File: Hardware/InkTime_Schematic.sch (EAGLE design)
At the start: 105 parts, among them IC1 RT6160AWSC, IC2 BMA423, IC3 BQ25180YBGR, IC4 DRV2605YZFR, J1 TC2030-IDC, J2 503480-2400, J4 KH-TYPE-C-16P_KH-TYPE-C-16P, Q1 20V/4.2A/52mΩ/1.4W, Q3 SI1308EDL-T1-GE3, U1 MAX17048G+T10, X1 32MHZ, X2 32.768KHZ

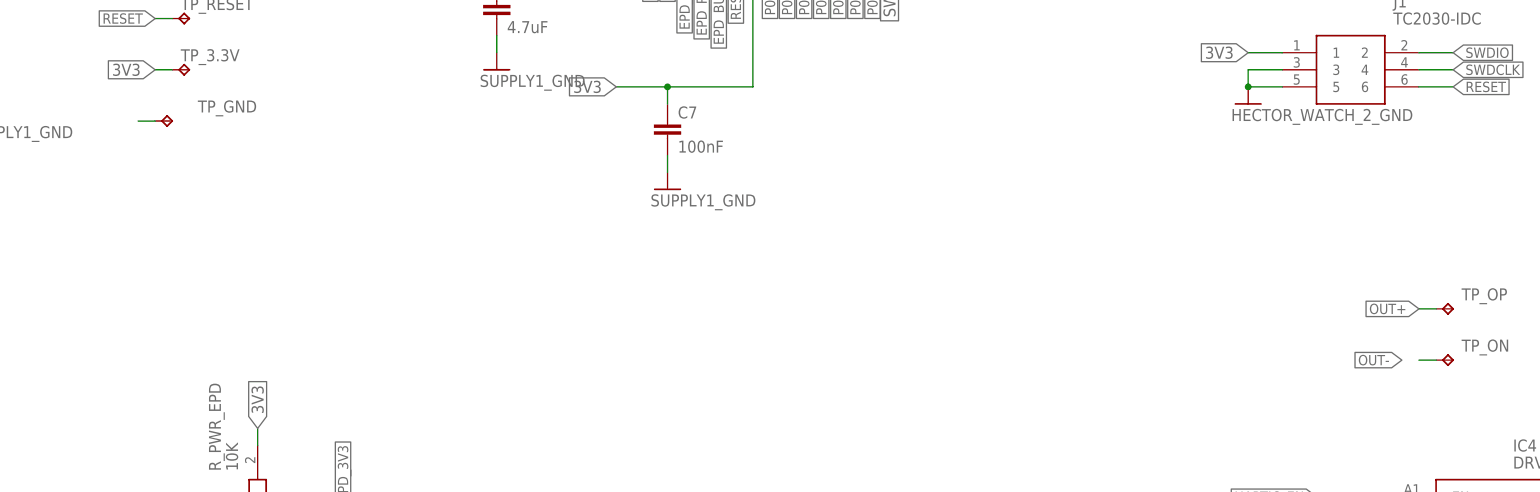
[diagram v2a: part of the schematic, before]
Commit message: Upated routing. Fixes #2, fixes #3, fixes #4, and resolves #5
Signed-off-by: Andrei Rusanescu <andreirusanescu154@gmail.com>
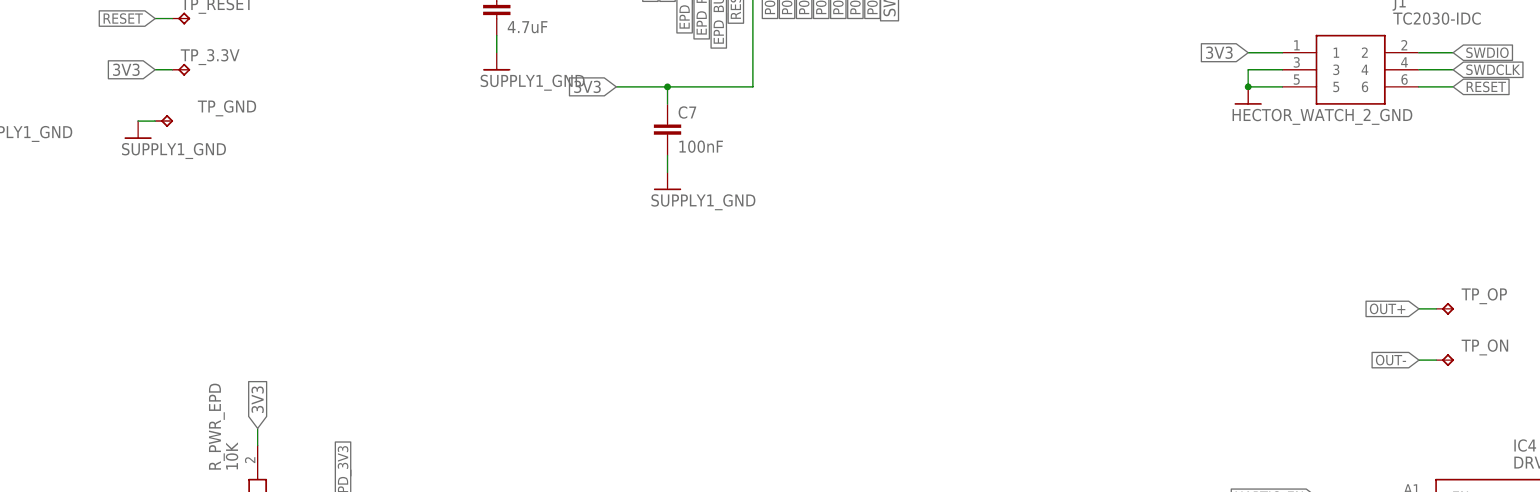
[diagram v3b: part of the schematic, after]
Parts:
- C19: SPICEPREFIX (none) -> C
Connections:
- removed net N$8: TP_GND.TP
- net GND: now also TP_GND.TP
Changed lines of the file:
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@@
 </classes>
 <parts>
-<part name="NRF52840_QF" library="InkTime_v5" deviceset="NORDIC_NRF_4_NRF52840_QF" device="" value="NRF52840_QF"/>
+<part uuid="0xABCDEF1A" name="NRF52840_QF" library="InkTime_v5" deviceset="NORDIC_NRF_4_NRF52840_QF" device="" value="NRF52840_QF"/>
 <part name="L1" library="InkTime_v5" deviceset="MLP2016SR47MT0S1_FTC252012SR47MBCA" device="" value="3.9nH"/>
 <part name="L2" library="InkTime_v5" deviceset="MLP2016SR47MT0S1_FTC252012SR47MBCA" device="" value="10uH"/>
 <part name="L3" library="InkTime_v5" deviceset="MLP2016SR47MT0S1_FTC252012SR47MBCA" device="" value="15nH"/>
-<part name="X1" library="InkTime_v5" deviceset="NORDIC_NRF_XTAL_32MHZ" device="" value="32MHZ"/>
+<part uuid="0xABCDEF0F" name="X1" library="InkTime_v5" deviceset="NORDIC_NRF_XTAL_32MHZ" device="" value="32MHZ"/>
 <part name="X2" library="InkTime_v5" deviceset="NORDIC_NRF_1_XTAL_32KHZ" device="" value="32.768KHZ"/>
-<part name="ANT1" library="InkTime_v5" deviceset="2450AT18B100E_2450AT18B100E" device="" value="2450AT18B100E"/>
-<part name="J1" library="InkTime_v5" deviceset="TC2030-IDC_TC2030-IDC" device="" value="TC2030-IDC"/>
-<part name="IC1" library="InkTime_v5" deviceset="RT6160AWSC_RT6160AWSC" device="" value="RT6160AWSC"/>
+<part uuid="0xABCDEF09" name="ANT1" library="InkTime_v5" deviceset="2450AT18B100E_2450AT18B100E" device="" value="2450AT18B100E"/>
+<part uuid="0xABCDEF18" name="J1" library="InkTime_v5" deviceset="TC2030-IDC_TC2030-IDC" device="" value="TC2030-IDC"/>
+<part uuid="0xABCDEF1C" name="IC1" library="InkTime_v5" deviceset="RT6160AWSC_RT6160AWSC" device="" value="RT6160AWSC"/>
 <part name="GND23" library="InkTime_v5" deviceset="HECTOR_WATCH_2_GND" device="" value="GND"/>
 <part name="R1" library="InkTime_v5" deviceset="CPF0201D7K68C1_CPF0201D7K68C1" device="" value="0"/>
@@
 <part name="TP_3.3V" library="InkTime_v5" deviceset="HECTOR_WATCH_1_TP" device="TP20R"/>
 <part name="TP_GND" library="InkTime_v5" deviceset="HECTOR_WATCH_1_TP" device="TP20R"/>
-<part name="IC2" library="InkTime_v5" deviceset="BMA423_BMA423" device="" value="BMA423"/>
+<part uuid="0xABCDEF1E" name="IC2" library="InkTime_v5" deviceset="BMA423_BMA423" device="" value="BMA423"/>
 <part name="R5" library="InkTime_v5" deviceset="CPF0201D7K68C1_CPF0201D7K68C1" device="" value="0"/>
-<part name="IC3" library="InkTime_v5" deviceset="BQ25180YBGR_BQ25180YBGR" device="" value="BQ25180YBGR"/>
+<part uuid="0xABCDEF02" name="IC3" library="InkTime_v5" deviceset="BQ25180YBGR_BQ25180YBGR" device="" value="BQ25180YBGR"/>
 <part name="R6" library="InkTime_v5" deviceset="CPF0201D7K68C1_CPF0201D7K68C1" device="" value="10K"/>
-<part name="D4" library="InkTime_v5" deviceset="ESP32_C6_LIBRARY_5_MBR0530" device="" value="MBR0530"/>
-<part name="D5" library="InkTime_v5" deviceset="ESP32_C6_LIBRARY_5_MBR0530" device="" value="MBR0530"/>
-<part name="D2" library="InkTime_v5" deviceset="ESP32_C6_LIBRARY_5_MBR0530" device="" value="MBR0530"/>
+<part uuid="0xABCDEF01" name="D4" library="InkTime_v5" deviceset="ESP32_C6_LIBRARY_5_MBR0530" device="" value="MBR0530"/>
+<part uuid="0xABCDEF05" name="D5" library="InkTime_v5" deviceset="ESP32_C6_LIBRARY_5_MBR0530" device="" value="MBR0530"/>
+<part uuid="0xABCDEF07" name="D2" library="InkTime_v5" deviceset="ESP32_C6_LIBRARY_5_MBR0530" device="" value="MBR0530"/>
 <part name="L5" library="InkTime_v5" deviceset="MLP2016SR47MT0S1_FTC252012SR47MBCA" device="" value="68uH"/>
-<part name="Q3" library="InkTime_v5" deviceset="ESP32_C6_LIBRARY_6_SI1308EDL-T1-GE3" device="" value="SI1308EDL-T1-GE3"/>
+<part uuid="0xABCDEF0B" name="Q3" library="InkTime_v5" deviceset="ESP32_C6_LIBRARY_6_SI1308EDL-T1-GE3" device="" value="SI1308EDL-T1-GE3"/>
 <part name="R2_EP_DR" library="InkTime_v5" deviceset="CPF0201D7K68C1_CPF0201D7K68C1" device="" value="10K"/>
 <part name="R1_EP_DR" library="InkTime_v5" deviceset="CPF0201D7K68C1_CPF0201D7K68C1" device="" value="0.47"/>
@@
 <part name="SJ1" library="InkTime_v5" deviceset="ESP32_C6_LIBRARY_7_JUMPER_SJ" device=""/>
 <part name="R_TYPE_SEL" library="InkTime_v5" deviceset="CPF0201D7K68C1_CPF0201D7K68C1" device="" value="2.2"/>
-<part name="Q1" library="InkTime_v5" deviceset="ESP32_C6_LIBRARY_4_ESP32_WROVER_SPARKFUN-DISCRETESEMI_MOSFET_PCH" device="-DMG2305UX-7" value="20V/4.2A/52mΩ/1.4W"/>
+<part uuid="0xABCDEF0D" name="Q1" library="InkTime_v5" deviceset="ESP32_C6_LIBRARY_4_ESP32_WROVER_SPARKFUN-DISCRETESEMI_MOSFET_PCH" device="-DMG2305UX-7" value="20V/4.2A/52mΩ/1.4W"/>
 <part name="R_PWR_EPD" library="InkTime_v5" deviceset="CPF0201D7K68C1_CPF0201D7K68C1" device="" value="10K"/>
-<part name="IC4" library="InkTime_v5" deviceset="DRV2605YZFR_DRV2605YZFR" device="" value="DRV2605YZFR"/>
+<part uuid="0xABCDEF14" name="IC4" library="InkTime_v5" deviceset="DRV2605YZFR_DRV2605YZFR" device="" value="DRV2605YZFR"/>
 <part name="TP_OP" library="InkTime_v5" deviceset="HECTOR_WATCH_1_TP" device="TP20R"/>
 <part name="TP_ON" library="InkTime_v5" deviceset="HECTOR_WATCH_1_TP" device="TP20R"/>
@@
 <part name="TP_VBAT" library="InkTime_v5" deviceset="HECTOR_WATCH_1_TP" device="TP20R"/>
 <part name="TP_BAT_GND" library="InkTime_v5" deviceset="HECTOR_WATCH_1_TP" device="TP20R"/>
-<part name="SW_UP" library="InkTime_v5" deviceset="2025-10-22_07-23-44_LIBRARY_EVP-AKE31A" device="SW_EVP-AKE31A_PAN" value="EVP-AKE31A_PAN"/>
+<part uuid="0xABCDEF13" name="SW_UP" library="InkTime_v5" deviceset="2025-10-22_07-23-44_LIBRARY_EVP-AKE31A" device="SW_EVP-AKE31A_PAN" value="EVP-AKE31A_PAN"/>
 <part name="R7" library="InkTime_v5" deviceset="CPF0201D7K68C1_CPF0201D7K68C1" device="" value="10k"/>
-<part name="SW_ENT" library="InkTime_v5" deviceset="2025-10-22_07-23-44_LIBRARY_EVP-AKE31A" device="SW_EVP-AKE31A_PAN" value="EVP-AKE31A_PAN"/>
+<part uuid="0xABCDEF11" name="SW_ENT" library="InkTime_v5" deviceset="2025-10-22_07-23-44_LIBRARY_EVP-AKE31A" device="SW_EVP-AKE31A_PAN" value="EVP-AKE31A_PAN"/>
 <part name="R8" library="InkTime_v5" deviceset="CPF0201D7K68C1_CPF0201D7K68C1" device="" value="10k"/>
-<part name="SW_DN" library="InkTime_v5" deviceset="2025-10-22_07-23-44_LIBRARY_EVP-AKE31A" device="SW_EVP-AKE31A_PAN" value="EVP-AKE31A_PAN"/>
+<part uuid="0xABCDEF17" name="SW_DN" library="InkTime_v5" deviceset="2025-10-22_07-23-44_LIBRARY_EVP-AKE31A" device="SW_EVP-AKE31A_PAN" value="EVP-AKE31A_PAN"/>
 <part name="R9" library="InkTime_v5" deviceset="CPF0201D7K68C1_CPF0201D7K68C1" device="" value="10k"/>
-<part name="J2" library="InkTime_v5" deviceset="503480-2400_503480-2400" device="" value="503480-2400"/>
-<part name="J4" library="InkTime_v5" deviceset="KH-TYPE-C-16P_KH-TYPE-C-16P" device=""/>
+<part uuid="0xABCDEF00" name="J2" library="InkTime_v5" deviceset="503480-2400_503480-2400" device="" value="503480-2400"/>
+<part uuid="0xABCDEF33" name="J4" library="InkTime_v5" deviceset="KH-TYPE-C-16P_KH-TYPE-C-16P" device=""/>
 <part name="R2_USB" library="InkTime_v5" deviceset="CPF0201D7K68C1_CPF0201D7K68C1" device="" value="5K1"/>
 <part name="R1_USB" library="InkTime_v5" deviceset="CPF0201D7K68C1_CPF0201D7K68C1" device="" value="5k1"/>
@@
 <part name="C33" library="InkTime_v5" deviceset="NORDIC_NRF_3_CAPACITOR" device="_0402_L" value="22uF"/>
 <part name="C23" library="InkTime_v5" deviceset="NORDIC_NRF_3_CAPACITOR" device="_0201_L" value="0.1uF"/>
-<part name="C19" library="InkTime_v5" deviceset="NORDIC_NRF_3_CAPACITOR" device="_0201_L" value="100nF"/>
+<part name="C19" library="InkTime_v5" deviceset="NORDIC_NRF_3_CAPACITOR" device="_0201_L" value="100nF">
+<attribute name="SPICEPREFIX" value="C"/>
+</part>
 <part name="C1-EP-DR" library="InkTime_v5" deviceset="NORDIC_NRF_3_CAPACITOR" device="_0402_L" value="10uF"/>
 <part name="C2-EP-DR" library="InkTime_v5" deviceset="NORDIC_NRF_3_CAPACITOR" device="_0402_L" value="4.7uF"/>
@@
 <part name="L7" library="InkTime_v5" deviceset="MLP2016SR47MT0S1_FTC252012SR47MBCA" device="" value="FTC252012SR47MBCA"/>
 <part name="GND33" library="InkTime_v5" deviceset="HECTOR_WATCH_2_GND" device=""/>
+<part name="GND34" library="InkTime_v5" deviceset="SUPPLY1_GND" device=""/>
 </parts>
 <sheets>
@@
 <instance part="GND33" gate="1" x="129.54" y="-12.7" smashed="yes">
 <attribute name="VALUE" x="127" y="-15.24" size="1.778" layer="96"/>
+</instance>
+<instance part="GND34" gate="1" x="-35.56" y="-17.78" smashed="yes">
+<attribute name="VALUE" x="-38.1" y="-20.32" size="1.778" layer="96"/>
 </instance>
 </instances>
@@
 <junction x="129.54" y="-10.16"/>
 </segment>
+<segment>
+<pinref part="TP_GND" gate="G$1" pin="TP"/>
+<wire x1="-33.02" y1="-15.24" x2="-35.56" y2="-15.24" width="0.1524" layer="91"/>
+<pinref part="GND34" gate="1" pin="GND"/>
+</segment>
 </net>
 <net name="N$4" class="2">
@@
 <pinref part="TP_ON" gate="G$1" pin="TP"/>
 <wire x1="157.48" y1="-50.8" x2="154.94" y2="-50.8" width="0.1524" layer="91"/>
-<label x="152.4" y="-50.8" size="1.524" layer="95" rot="R180" xref="yes"/>
+<label x="154.94" y="-50.8" size="1.524" layer="95" rot="R180" xref="yes"/>
 </segment>
 </net>
@@
 </segment>
 </net>
-<net name="N$8" class="2">
-<segment>
-<pinref part="TP_GND" gate="G$1" pin="TP"/>
-<wire x1="-33.02" y1="-15.24" x2="-35.56" y2="-15.24" width="0.1524" layer="91"/>
-</segment>
-</net>
